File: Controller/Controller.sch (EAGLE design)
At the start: 0 parts

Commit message: Modified controller.
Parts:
- added FRAME1: FRAME-LETTER, SparkFun-Aesthetics:FRAME-LETTER
- added U1: TPD4S009DBVR, Texas Instruments_By_element14_Batch_1:TPD4S009DBVR
- added U2: TPS2511DGN, TI-TPS2511DGN:TPS2511DGN
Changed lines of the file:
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@@
 <grid distance="0.1" unitdist="inch" unit="inch" style="lines" multiple="1" display="no" altdistance="0.01" altunitdist="inch" altunit="inch"/>
 <layers>
+<layer number="1" name="Top" color="4" fill="1" visible="no" active="no"/>
+<layer number="16" name="Bottom" color="1" fill="1" visible="no" active="no"/>
+<layer number="17" name="Pads" color="2" fill="1" visible="no" active="no"/>
+<layer number="18" name="Vias" color="2" fill="1" visible="no" active="no"/>
+<layer number="19" name="Unrouted" color="6" fill="1" visible="no" active="no"/>
+<layer number="20" name="Dimension" color="15" fill="1" visible="no" active="no"/>
+<layer number="21" name="tPlace" color="7" fill="1" visible="no" active="no"/>
+<layer number="22" name="bPlace" color="7" fill="1" visible="no" active="no"/>
+<layer number="23" name="tOrigins" color="15" fill="1" visible="no" active="no"/>
+<layer number="24" name="bOrigins" color="15" fill="1" visible="no" active="no"/>
+<layer number="25" name="tNames" color="7" fill="1" visible="no" active="no"/>
+<layer number="26" name="bNames" color="7" fill="1" visible="no" active="no"/>
+<layer number="27" name="tValues" color="7" fill="1" visible="no" active="no"/>
+<layer number="28" name="bValues" color="7" fill="1" visible="no" active="no"/>
+<layer number="29" name="tStop" color="7" fill="3" visible="no" active="no"/>
+<layer number="30" name="bStop" color="7" fill="6" visible="no" active="no"/>
+<layer number="31" name="tCream" color="7" fill="4" visible="no" active="no"/>
+<layer number="32" name="bCream" color="7" fill="5" visible="no" active="no"/>
+<layer number="33" name="tFinish" color="6" fill="3" visible="no" active="no"/>
+<layer number="34" name="bFinish" color="6" fill="6" visible="no" active="no"/>
+<layer number="35" name="tGlue" color="7" fill="4" visible="no" active="no"/>
+<layer number="36" name="bGlue" color="7" fill="5" visible="no" active="no"/>
+<layer number="37" name="tTest" color="7" fill="1" visible="no" active="no"/>
+<layer number="38" name="bTest" color="7" fill="1" visible="no" active="no"/>
+<layer number="39" name="tKeepout" color="4" fill="11" visible="no" active="no"/>
+<layer number="40" name="bKeepout" color="1" fill="11" visible="no" active="no"/>
+<layer number="41" name="tRestrict" color="4" fill="10" visible="no" active="no"/>
+<layer number="42" name="bRestrict" color="1" fill="10" visible="no" active="no"/>
+<layer number="43" name="vRestrict" color="2" fill="10" visible="no" active="no"/>
+<layer number="44" name="Drills" color="7" fill="1" visible="no" active="no"/>
+<layer number="45" name="Holes" color="7" fill="1" visible="no" active="no"/>
+<layer number="46" name="Milling" color="3" fill="1" visible="no" active="no"/>
+<layer number="47" name="Measures" color="7" fill="1" visible="no" active="no"/>
+<layer number="48" name="Document" color="7" fill="1" visible="no" active="no"/>
+<layer number="49" name="Reference" color="7" fill="1" visible="no" active="no"/>
+<layer number="50" name="dxf" color="7" fill="1" visible="no" active="no"/>
+<layer number="51" name="tDocu" color="7" fill="1" visible="no" active="no"/>
+<layer number="52" name="bDocu" color="7" fill="1" visible="no" active="no"/>
+<layer number="53" name="tGND_GNDA" color="7" fill="9" visible="no" active="no"/>
+<layer number="54" name="bGND_GNDA" color="1" fill="9" visible="no" active="no"/>
+<layer number="56" name="wert" color="7" fill="1" visible="no" active="no"/>
 <layer number="90" name="Modules" color="5" fill="1" visible="yes" active="yes"/>
 <layer number="91" name="Nets" color="2" fill="1" visible="yes" active="yes"/>
@@
 <layer number="97" name="Info" color="7" fill="1" visible="yes" active="yes"/>
 <layer number="98" name="Guide" color="6" fill="1" visible="yes" active="yes"/>
+<layer number="100" name="Muster" color="7" fill="1" visible="no" active="no"/>
+<layer number="101" name="Patch_Top" color="12" fill="4" visible="yes" active="yes"/>
+<layer number="102" name="Vscore" color="7" fill="1" visible="yes" active="yes"/>
+<layer number="103" name="tMap" color="7" fill="1" visible="yes" active="yes"/>
+<layer number="104" name="Name" color="16" fill="1" visible="yes" active="yes"/>
+<layer number="105" name="tPlate" color="7" fill="1" visible="yes" active="yes"/>
+<layer number="106" name="bPlate" color="7" fill="1" visible="yes" active="yes"/>
+<layer number="107" name="Crop" color="7" fill="1" visible="yes" active="yes"/>
+<layer number="108" name="tplace-old" color="10" fill="1" visible="no" active="yes"/>
+<layer number="109" name="ref-old" color="11" fill="1" visible="no" active="yes"/>
+<layer number="116" name="Patch_BOT" color="9" fill="4" visible="yes" active="yes"/>
+<layer number="121" name="_tsilk" color="7" fill="1" visible="yes" active="yes"/>
+<layer number="122" name="_bsilk" color="7" fill="1" visible="yes" active="yes"/>
+<layer number="125" name="_tNames" color="7" fill="1" visible="yes" active="yes"/>
+<layer number="144" name="Drill_legend" color="7" fill="1" visible="yes" active="yes"/>
+<layer number="151" name="HeatSink" color="7" fill="1" visible="yes" active="yes"/>
+<layer number="199" name="Contour" color="7" fill="1" visible="yes" active="yes"/>
+<layer number="200" name="200bmp" color="1" fill="10" visible="yes" active="yes"/>
+<layer number="201" name="201bmp" color="2" fill="10" visible="yes" active="yes"/>
+<layer number="202" name="202bmp" color="3" fill="10" visible="yes" active="yes"/>
+<layer number="203" name="203bmp" color="4" fill="10" visible="yes" active="yes"/>
+<layer number="204" name="204bmp" color="5" fill="10" visible="yes" active="yes"/>
+<layer number="205" name="205bmp" color="6" fill="10" visible="yes" active="yes"/>
+<layer number="206" name="206bmp" color="7" fill="10" visible="yes" active="yes"/>
+<layer number="207" name="207bmp" color="8" fill="10" visible="yes" active="yes"/>
+<layer number="208" name="208bmp" color="9" fill="10" visible="yes" active="yes"/>
+<layer number="209" name="209bmp" color="7" fill="1" visible="yes" active="yes"/>
+<layer number="210" name="210bmp" color="7" fill="1" visible="yes" active="yes"/>
+<layer number="211" name="211bmp" color="7" fill="1" visible="yes" active="yes"/>
+<layer number="212" name="212bmp" color="7" fill="1" visible="yes" active="yes"/>
+<layer number="213" name="213bmp" color="7" fill="1" visible="yes" active="yes"/>
+<layer number="214" name="214bmp" color="7" fill="1" visible="yes" active="yes"/>
+<layer number="215" name="215bmp" color="7" fill="1" visible="yes" active="yes"/>
+<layer number="216" name="216bmp" color="7" fill="1" visible="yes" active="yes"/>
+<layer number="217" name="217bmp" color="18" fill="1" visible="no" active="no"/>
+<layer number="218" name="218bmp" color="19" fill="1" visible="no" active="no"/>
+<layer number="219" name="219bmp" color="20" fill="1" visible="no" active="no"/>
+<layer number="220" name="220bmp" color="21" fill="1" visible="no" active="no"/>
+<layer number="221" name="221bmp" color="22" fill="1" visible="no" active="no"/>
+<layer number="222" name="222bmp" color="23" fill="1" visible="no" active="no"/>
+<layer number="223" name="223bmp" color="24" fill="1" visible="no" active="no"/>
+<layer number="224" name="224bmp" color="25" fill="1" visible="no" active="no"/>
+<layer number="250" name="Descript" color="3" fill="1" visible="no" active="no"/>
+<layer number="251" name="SMDround" color="12" fill="11" visible="no" active="no"/>
+<layer number="254" name="cooling" color="7" fill="1" visible="yes" active="yes"/>
 </layers>
 <schematic xreflabel="%F%N/%S.%C%R" xrefpart="/%S.%C%R">
@@
 </classes>
 <parts>
+<part name="FRAME1" library="SparkFun-Aesthetics" deviceset="FRAME-LETTER" device=""/>
+<part name="U1" library="Texas Instruments_By_element14_Batch_1" deviceset="TPD4S009DBVR" device=""/>
+<part name="U2" library="TI-TPS2511DGN" deviceset="TPS2511DGN" device=""/>
 </parts>
 <sheets>
@@
 </plain>
 <instances>
+<instance part="FRAME1" gate="G$1" x="0.786075" y="0"/>
+<instance part="FRAME1" gate="G$2" x="148.106075" y="0"/>
+<instance part="U1" gate="A" x="76.2" y="134.62"/>
+<instance part="U2" gate="A" x="165.1" y="127"/>
 </instances>
 <busses>

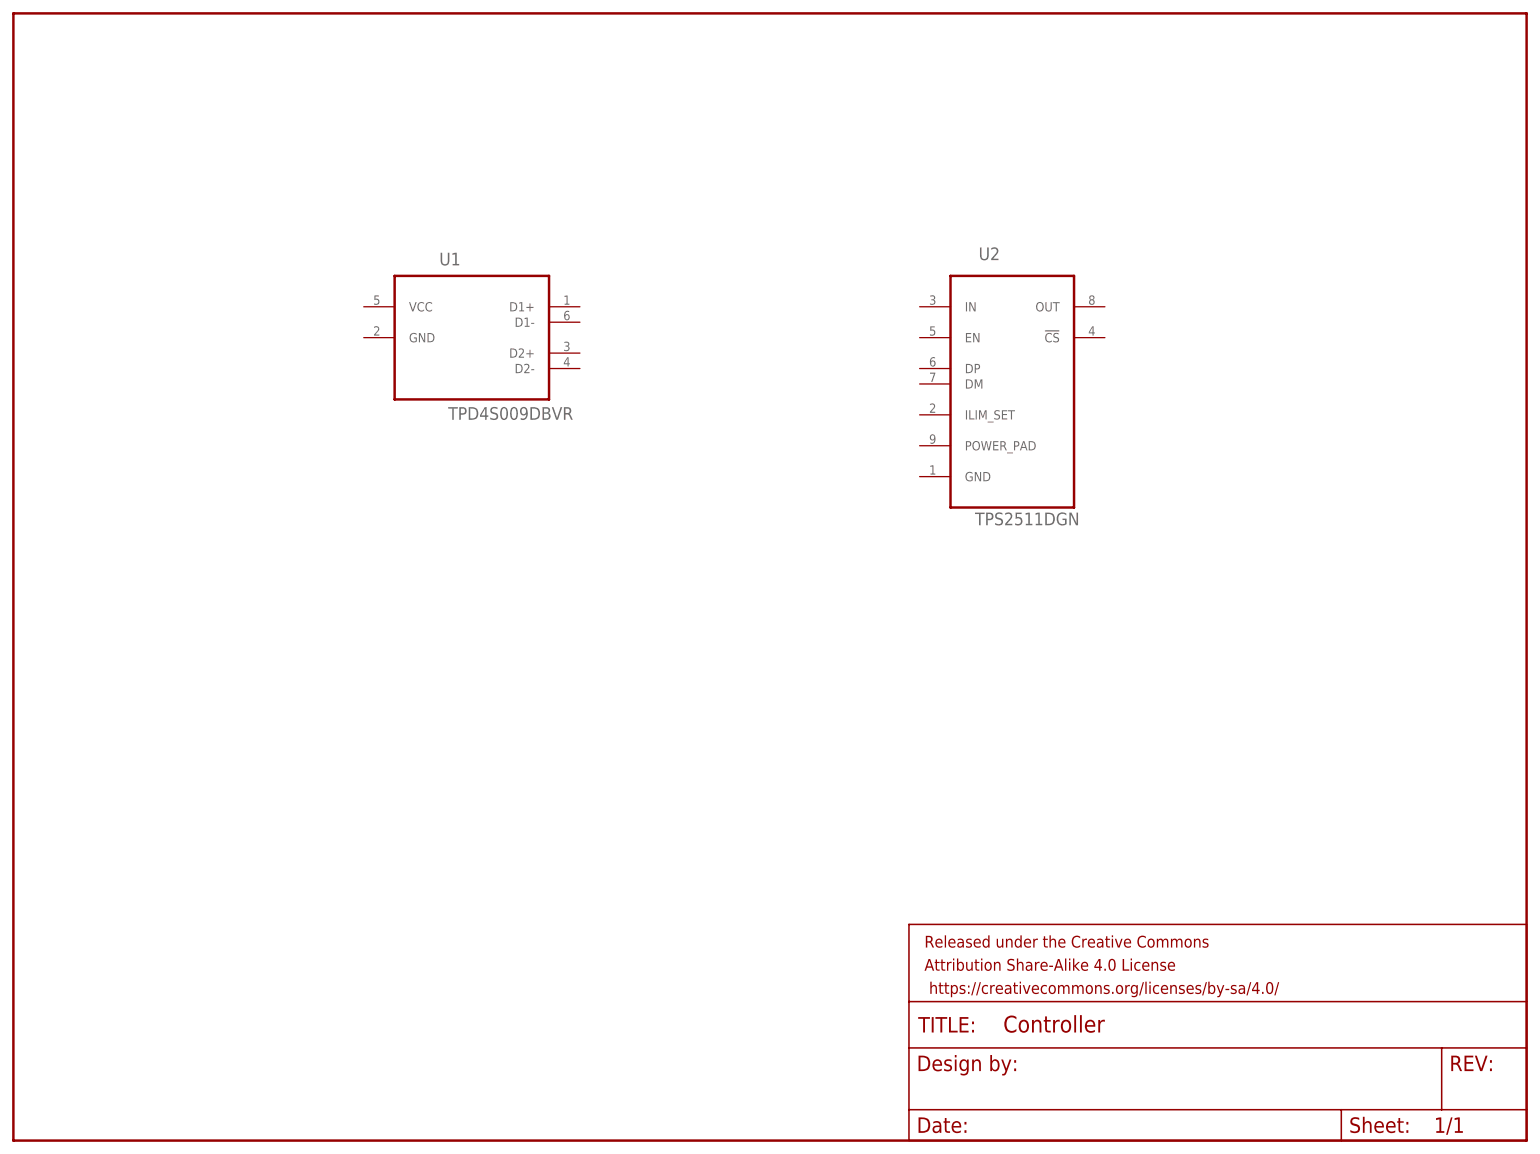
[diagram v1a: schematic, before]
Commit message: Modified ESD/Controller board and schematic.
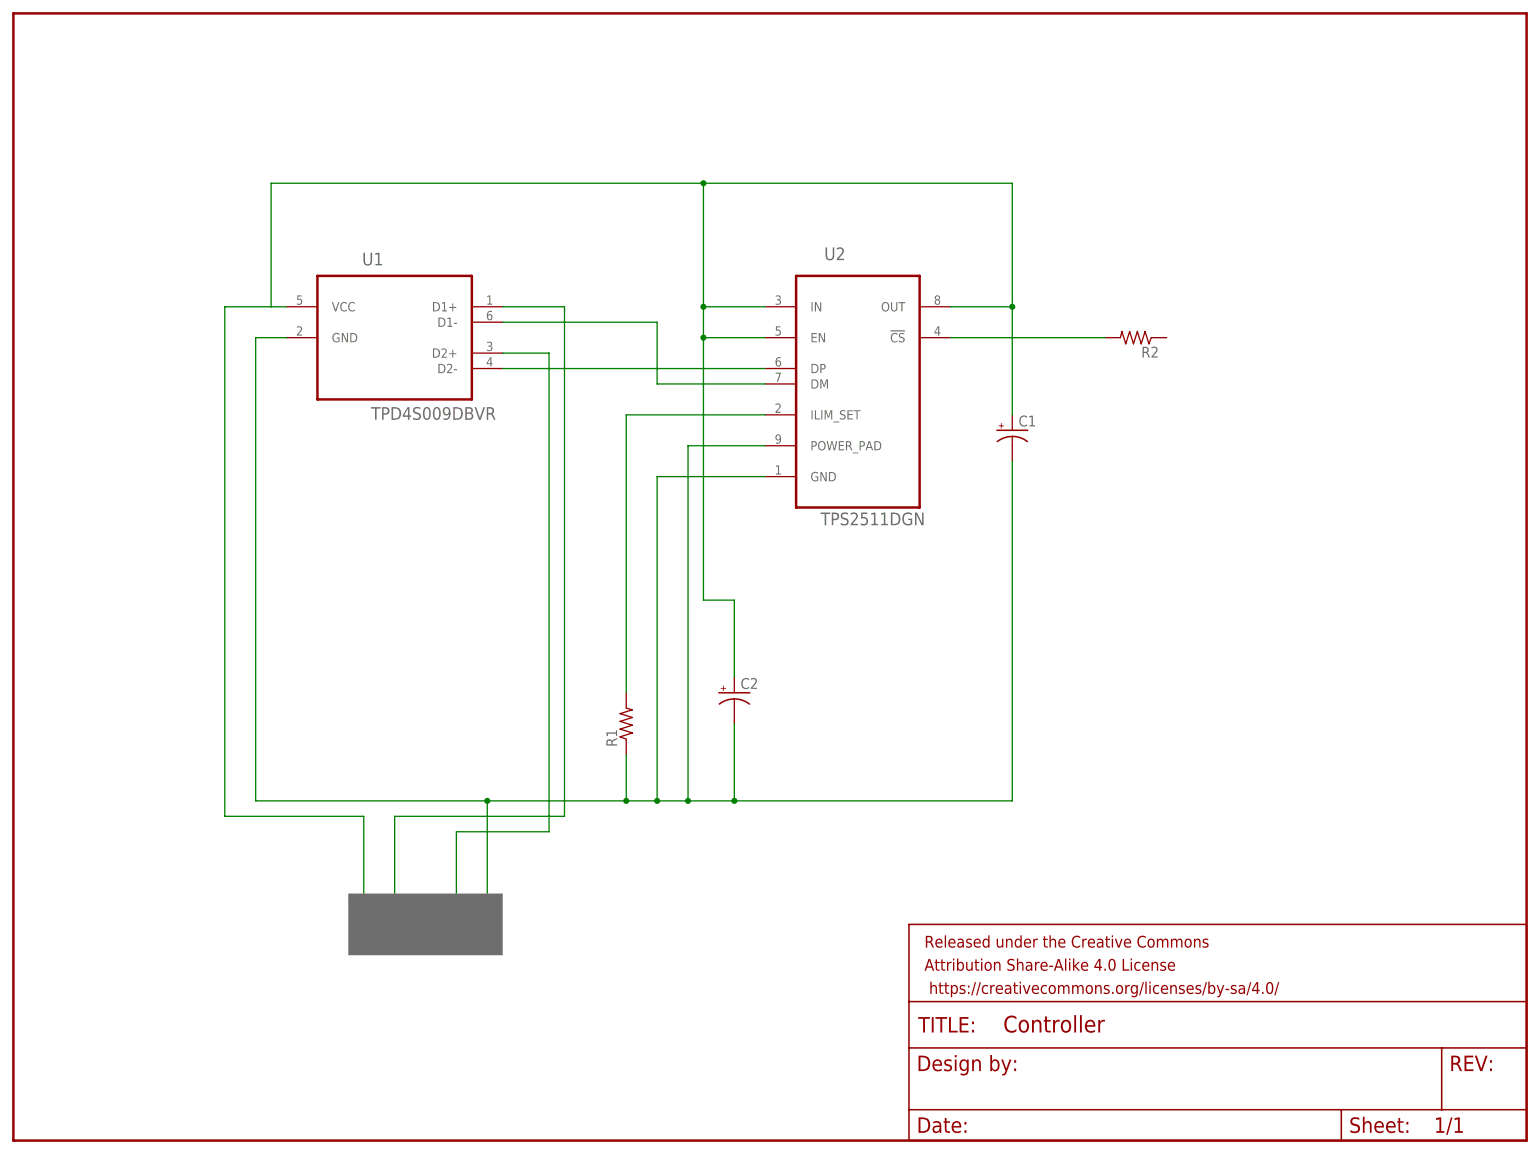
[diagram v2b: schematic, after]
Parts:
- added C1, C2: (no value), adafruit:CPOL-USE2-5
- added R1, R2: (no value), SparkFun-Passives:RESISTORKIT
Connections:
- new net N$1: U1.D2+
- new net N$2: U1.D1+
- new net N$3: C1.+, C2.+, U1.VCC, U2.EN, U2.IN, U2.OUT
- new net N$4: C1.-, C2.-, R1.1, U1.GND, U2.GND, U2.POWER_PAD
- new net N$5: U1.D1-, U2.DM
- new net N$6: U1.D2-, U2.DP
- new net N$7: R1.2, U2.ILIM_SET
- new net N$8: R2.2, U2.!CS
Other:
- note added: "DATA+"
- note added: "DATA-"
- note added: "GND"
- note added: "VCC"
- moved on the sheet: U1, U2
